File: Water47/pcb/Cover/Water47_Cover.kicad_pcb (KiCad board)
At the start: 2 copper layers, 260 x 25.6 mm, 2 parts

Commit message: feat: add mounting holes
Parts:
- added H2: MountingHole, kbd_Hole:m2_Screw_Hole, F.Cu at (85.0, 104.8)
- added H4: MountingHole, kbd_Hole:m2_Screw_Hole, F.Cu at (339.0, 104.8)
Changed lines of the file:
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@@
+  )
+  (footprint "kbd_Hole:m2_Screw_Hole" (layer "F.Cu")
+    (at 85 104.8)
+    (descr "Mounting Hole 2.2mm, no annular, M2")
+    (tags "mounting hole 2.2mm no annular m2")
+    (property "Sheetfile" "Water47_Cover.kicad_sch")
+    (property "Sheetname" "")
+    (attr exclude_from_pos_files)
+    (fp_text reference "H2" (at 0 -3.2) (layer "F.Fab")
+      (effects (font (size 1 1) (thickness 0.15)))
+    )
+    (fp_text value "MountingHole" (at 0 3.2) (layer "F.Fab")
+      (effects (font (size 1 1) (thickness 0.15)))
+    )
+    (fp_text user "${REFERENCE}" (at 0.3 0) (layer "F.Fab")
+      (effects (font (size 1 1) (thickness 0.15)))
+    )
+    (fp_circle (center 0 0) (end 2.2 0) (layer "Cmts.User") (width 0.15) (fill none))
+    (fp_circle (center 0 0) (end 2.45 0) (layer "F.CrtYd") (width 0.05) (fill none))
+    (pad "" np_thru_hole circle locked (at 0 0) (size 2.2 2.2) (drill 2.2) (layers *.Cu *.Mask))
+  )
+  (footprint "kbd_Hole:m2_Screw_Hole" (layer "F.Cu")
+    (at 339 104.8)
+    (descr "Mounting Hole 2.2mm, no annular, M2")
+    (tags "mounting hole 2.2mm no annular m2")
+    (property "Sheetfile" "Water47_Cover.kicad_sch")
+    (property "Sheetname" "")
+    (attr exclude_from_pos_files)
+    (fp_text reference "H4" (at 0 -3.2) (layer "F.Fab")
+      (effects (font (size 1 1) (thickness 0.15)))
+    )
+    (fp_text value "MountingHole" (at 0 3.2) (layer "F.Fab")
+      (effects (font (size 1 1) (thickness 0.15)))
+    )
+    (fp_text user "${REFERENCE}" (at 0.3 0) (layer "F.Fab")
+      (effects (font (size 1 1) (thickness 0.15)))
+    )
+    (fp_circle (center 0 0) (end 2.2 0) (layer "Cmts.User") (width 0.15) (fill none))
+    (fp_circle (center 0 0) (end 2.45 0) (layer "F.CrtYd") (width 0.05) (fill none))
+    (pad "" np_thru_hole circle locked (at 0 0) (size 2.2 2.2) (drill 2.2) (layers *.Cu *.Mask))
   )
   (footprint "kbd_Hole:m2_Screw_Hole" (layer "F.Cu")

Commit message: feat: add logo
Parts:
- added G***: LOGO, Silk_Wizard_logos:silk_wizard_logo_60x60, B.Cu at (212.0, 121.5)

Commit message: feat: increase logo size
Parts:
- G***: footprint Silk_Wizard_logos:silk_wizard_logo_60x60 -> Silk_Wizard_logos:silk_wizard_logo_70x70

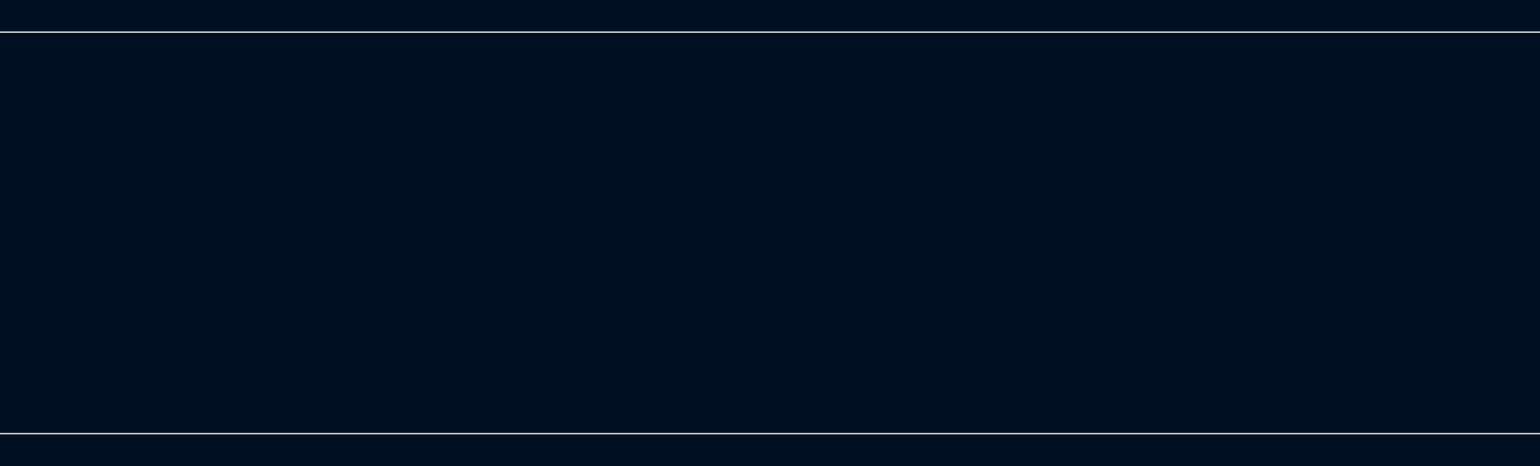
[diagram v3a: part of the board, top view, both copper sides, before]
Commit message: feat: add mounting hole, set gerber path
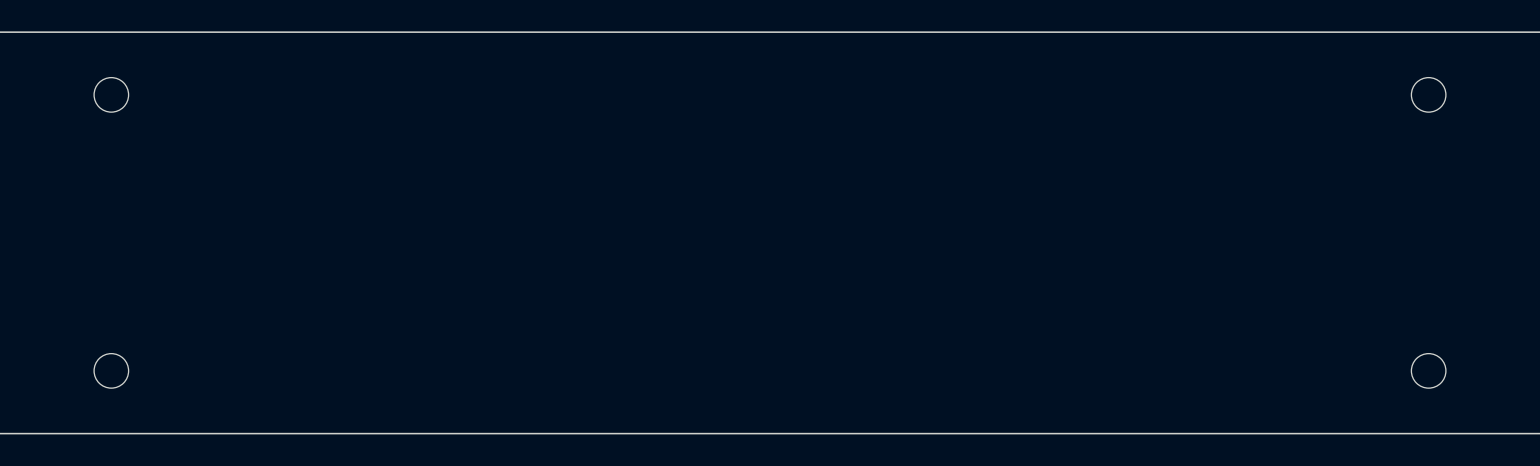
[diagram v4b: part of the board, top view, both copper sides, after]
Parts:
- added H5: MountingHole, kbd_Hole:m2_Screw_Hole, F.Cu at (85.0, 104.8)
- added H6: MountingHole, kbd_Hole:m2_Screw_Hole, F.Cu at (170.0, 104.8)
- added H7: MountingHole, kbd_Hole:m2_Screw_Hole, F.Cu at (254.0, 104.8)
- added H8: MountingHole, kbd_Hole:m2_Screw_Hole, F.Cu at (339.0, 104.8)
- moved H2 86.8 mm to (170.0, 87.2)
- moved H3 85.0 mm to (254.0, 87.2)
- moved H4 17.6 mm to (339.0, 87.2)
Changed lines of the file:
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@@
       (drillshape 0)
       (scaleselection 1)
-      (outputdirectory "../../gerber/PCB_Layer1/")
+      (outputdirectory "../../gerber/04Cover/")
     )
   )
   (net 0 "")
+  (footprint "kbd_Hole:m2_Screw_Hole" (layer "F.Cu")
+    (at 339 104.8)
+    (descr "Mounting Hole 2.2mm, no annular, M2")
+    (tags "mounting hole 2.2mm no annular m2")
+    (property "Sheetfile" "Water47_Cover.kicad_sch")
+    (property "Sheetname" "")
+    (attr exclude_from_pos_files)
+    (fp_text reference "H8" (at 0 -3.2) (layer "F.Fab")
+      (effects (font (size 1 1) (thickness 0.15)))
+    )
+    (fp_text value "MountingHole" (at 0 3.2) (layer "F.Fab")
+      (effects (font (size 1 1) (thickness 0.15)))
+    )
+    (fp_text user "${REFERENCE}" (at 0.3 0) (layer "F.Fab")
+      (effects (font (size 1 1) (thickness 0.15)))
+    )
+    (fp_circle (center 0 0) (end 2.2 0) (layer "Cmts.User") (width 0.15) (fill none))
+    (fp_circle (center 0 0) (end 2.45 0) (layer "F.CrtYd") (width 0.05) (fill none))
+    (pad "" np_thru_hole circle locked (at 0 0) (size 2.2 2.2) (drill 2.2) (layers *.Cu *.Mask))
+  )
   (footprint "kbd_Hole:m2_Screw_Hole" (layer "F.Cu")
     (at 85 87.2)
@@
     (property "Sheetname" "")
     (attr exclude_from_pos_files)
+    (fp_text reference "H5" (at 0 -3.2) (layer "F.Fab")
+      (effects (font (size 1 1) (thickness 0.15)))
+    )
+    (fp_text value "MountingHole" (at 0 3.2) (layer "F.Fab")
+      (effects (font (size 1 1) (thickness 0.15)))
+    )
+    (fp_text user "${REFERENCE}" (at 0.3 0) (layer "F.Fab")
+      (effects (font (size 1 1) (thickness 0.15)))
+    )
+    (fp_circle (center 0 0) (end 2.2 0) (layer "Cmts.User") (width 0.15) (fill none))
+    (fp_circle (center 0 0) (end 2.45 0) (layer "F.CrtYd") (width 0.05) (fill none))
+    (pad "" np_thru_hole circle locked (at 0 0) (size 2.2 2.2) (drill 2.2) (layers *.Cu *.Mask))
+  )
+  (footprint "kbd_Hole:m2_Screw_Hole" (layer "F.Cu")
+    (at 170 87.2)
+    (descr "Mounting Hole 2.2mm, no annular, M2")
+    (tags "mounting hole 2.2mm no annular m2")
+    (property "Sheetfile" "Water47_Cover.kicad_sch")
+    (property "Sheetname" "")
+    (attr exclude_from_pos_files)
     (fp_text reference "H2" (at 0 -3.2) (layer "F.Fab")
       (effects (font (size 1 1) (thickness 0.15)))
@@
   )
   (footprint "kbd_Hole:m2_Screw_Hole" (layer "F.Cu")
-    (at 339 104.8)
+    (at 339 87.2)
     (descr "Mounting Hole 2.2mm, no annular, M2")
     (tags "mounting hole 2.2mm no annular m2")
@@
   )
   (footprint "kbd_Hole:m2_Screw_Hole" (layer "F.Cu")
-    (at 339 87.2)
+    (at 170 104.8)
     (descr "Mounting Hole 2.2mm, no annular, M2")
     (tags "mounting hole 2.2mm no annular m2")
+    (property "Sheetfile" "Water47_Cover.kicad_sch")
+    (property "Sheetname" "")
+    (attr exclude_from_pos_files)
+    (fp_text reference "H6" (at 0 -3.2) (layer "F.Fab")
+      (effects (font (size 1 1) (thickness 0.15)))
+    )
+    (fp_text value "MountingHole" (at 0 3.2) (layer "F.Fab")
+      (effects (font (size 1 1) (thickness 0.15)))
+    )
+    (fp_text user "${REFERENCE}" (at 0.3 0) (layer "F.Fab")
+      (effects (font (size 1 1) (thickness 0.15)))
+    )
+    (fp_circle (center 0 0) (end 2.2 0) (layer "Cmts.User") (width 0.15) (fill none))
+    (fp_circle (center 0 0) (end 2.45 0) (layer "F.CrtYd") (width 0.05) (fill none))
+    (pad "" np_thru_hole circle locked (at 0 0) (size 2.2 2.2) (drill 2.2) (layers *.Cu *.Mask))
+  )
+  (footprint "kbd_Hole:m2_Screw_Hole" (layer "F.Cu")
+    (at 254 104.8)
+    (descr "Mounting Hole 2.2mm, no annular, M2")
+    (tags "mounting hole 2.2mm no annular m2")
+    (property "Sheetfile" "Water47_Cover.kicad_sch")
+    (property "Sheetname" "")
+    (attr exclude_from_pos_files)
+    (fp_text reference "H7" (at 0 -3.2) (layer "F.Fab")
+      (effects (font (size 1 1) (thickness 0.15)))
+    )
+    (fp_text value "MountingHole" (at 0 3.2) (layer "F.Fab")
+      (effects (font (size 1 1) (thickness 0.15)))
+    )
+    (fp_text user "${REFERENCE}" (at 0.3 0) (layer "F.Fab")
+      (effects (font (size 1 1) (thickness 0.15)))
+    )
+    (fp_circle (center 0 0) (end 2.2 0) (layer "Cmts.User") (width 0.15) (fill none))
+    (fp_circle (center 0 0) (end 2.45 0) (layer "F.CrtYd") (width 0.05) (fill none))
+    (pad "" np_thru_hole circle locked (at 0 0) (size 2.2 2.2) (drill 2.2) (layers *.Cu *.Mask))
+  )
+  (footprint "kbd_Hole:m2_Screw_Hole" (layer "F.Cu")
+    (at 254 87.2)
+    (descr "Mounting Hole 2.2mm, no annular, M2")
+    (tags "mounting hole 2.2mm no annular m2")

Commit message: fix: invisible redundant silkscreen
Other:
- board text added: "Water47 ver1.1 @Cover Designed by multifeb13"
- board text removed: "Water47 ver1.0 @Cover Designed by multifeb13"
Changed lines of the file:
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@@
     (at 212 121.45 180)
     (attr board_only exclude_from_pos_files exclude_from_bom)
-    (fp_text reference "G***" (at 0 0) (layer "B.SilkS")
+    (fp_text reference "G***" (at 0 0) (layer "B.SilkS") hide
       (effects (font (size 1.524 1.524) (thickness 0.3)) (justify mirror))
     )
@@
   (gr_line (start 340 83.2) (end 84 83.2) (layer "Edge.Cuts") (width 0.1))
   (gr_arc (start 84 108.8) (mid 82.585786 108.214214) (end 82 106.8) (layer "Edge.Cuts") (width 0.1))
-  (gr_text "Water47 ver1.0 @Cover Designed by multifeb13" (at 335 107) (layer "F.SilkS")
+  (gr_text "Water47 ver1.1 @Cover Designed by multifeb13" (at 335 107) (layer "F.SilkS")
     (effects (font (size 1 1) (thickness 0.125)) (justify right))
   )
